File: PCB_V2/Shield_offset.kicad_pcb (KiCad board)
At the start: 4 copper layers, 83.2 x 79.4 mm, 120 parts, among them J1 ADC, J10 I2C, J11 SERVO3, J12 SERVO4, J13 Power OUT, J2 BATT, J3 PWR SW, J4 Screw_Terminal_01x04, J5 SERVO1, J6 ULTRA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

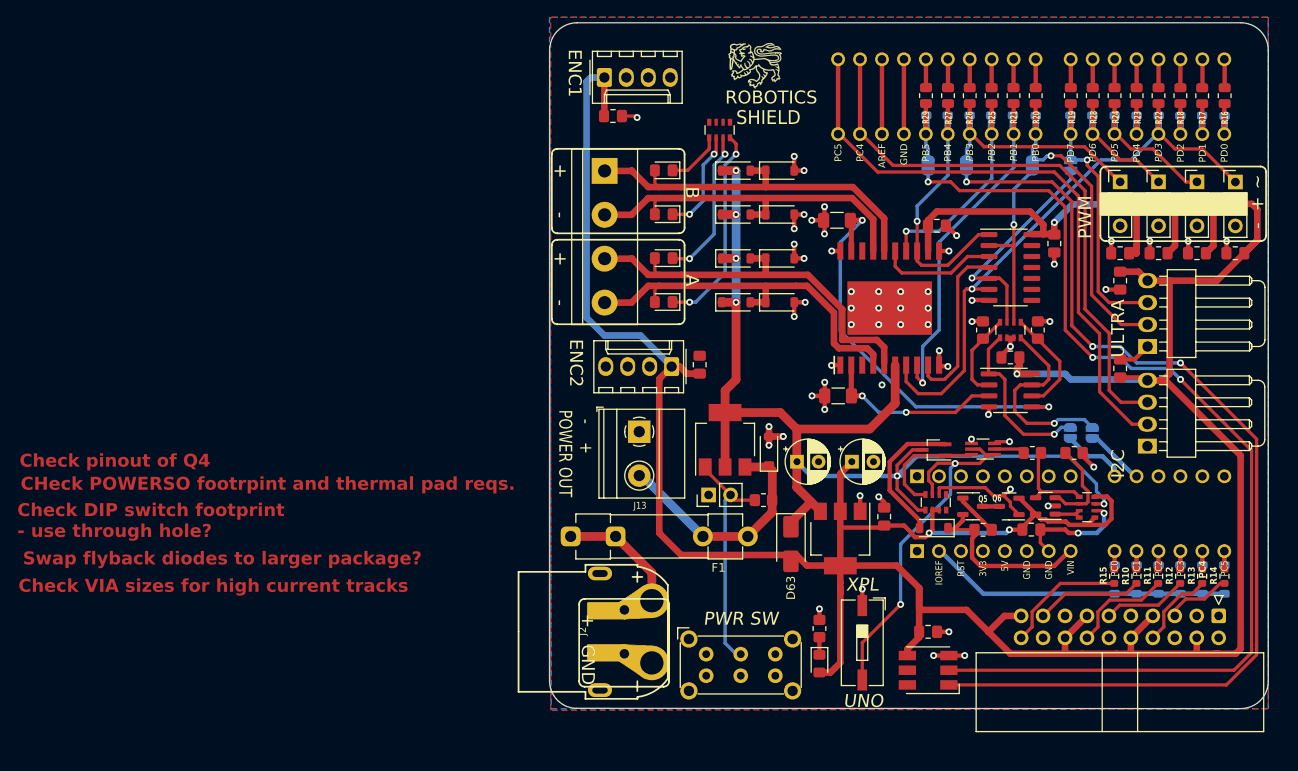
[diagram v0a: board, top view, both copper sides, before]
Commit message: Minor changes to layout
fixed overlapping silk and courtyards
tweaked track layouts to clear disconencted edges and imporve some clearances
fixed board outline
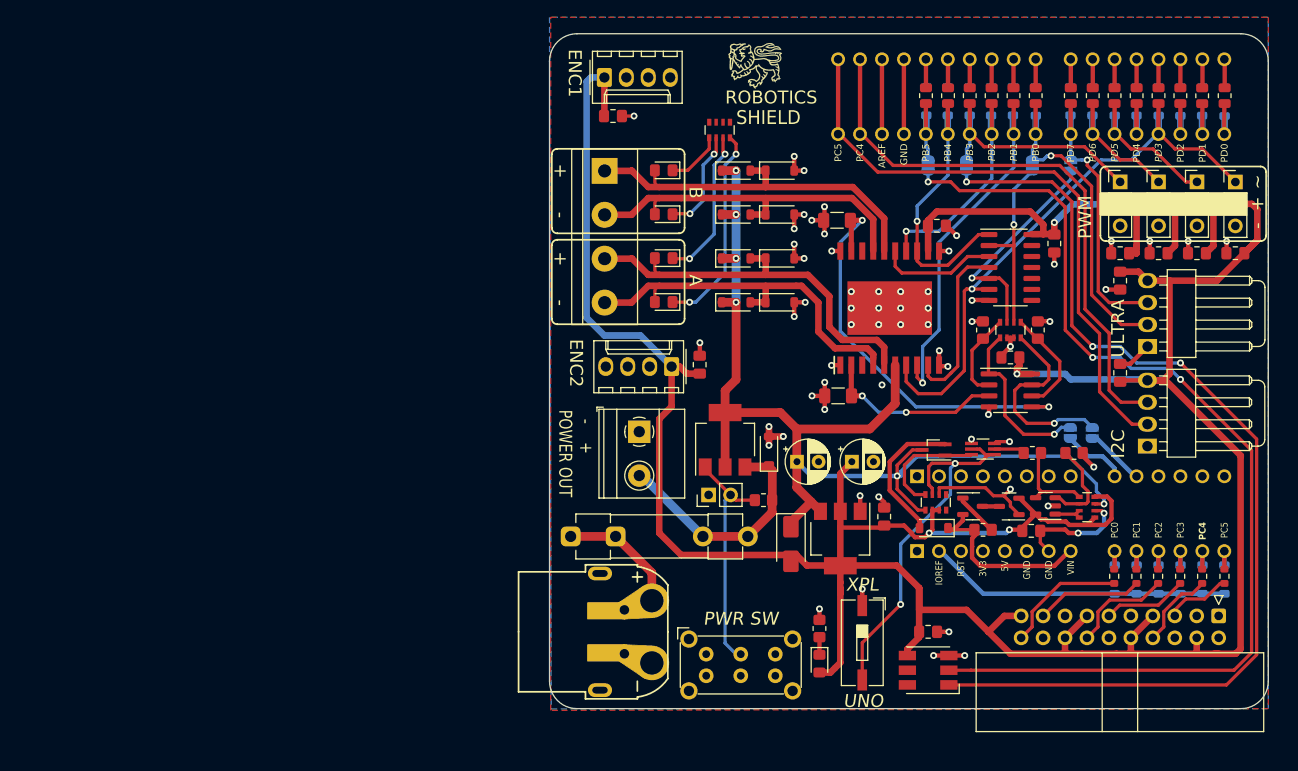
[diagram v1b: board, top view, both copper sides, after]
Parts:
- moved C12 0.51 mm to (158.8, 61.5)
- moved C6 0.15 mm to (148.5, 79.8)
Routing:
- net GND: track 107.7 -> 109.5 mm, vias 60 -> 61
- net /AIN5: track 10.2 -> 11.8 mm
- net /AIN3: track 10.4 -> 12.0 mm
- net /AIN2: track 10.4 -> 12.0 mm
- net /AIN0: track 18.1 -> 19.7 mm
- net /AIN1: track 17.4 -> 19.0 mm
- net /AIN4: track 10.8 -> 12.0 mm
- net /ENC2B: track 87.8 -> 88.9 mm
- net Net-(J3-Pin_2): track 27.7 -> 26.8 mm
- net +5V: track 408.0 -> 407.3 mm
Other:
- board size 83.2 x 79.4 mm -> 83.2 x 78.1 mm
- board text removed: "CHeck POWERSO footrpint and thermal pad reqs."
- board text removed: "Check DIP switch footprint - use through hole?"
- board text removed: "Check VIA sizes for high current tracks"
- board text removed: "Check pinout of Q4"
- board text removed: "Swap flyback diodes to larger package?"

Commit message: Update
Added gnd via's, and caps for LP filter on analog in's
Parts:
- added C17: NL, Capacitor_SMD:C_0805_2012Metric_Pad1.18x1.45mm_HandSolder, B.Cu at (158.8, 78.7)
- added C18: NL, Capacitor_SMD:C_0805_2012Metric_Pad1.18x1.45mm_HandSolder, B.Cu at (161.3, 78.7)
- added C19: NL, Capacitor_SMD:C_0805_2012Metric_Pad1.18x1.45mm_HandSolder, B.Cu at (163.8, 78.7)
- added C20: NL, Capacitor_SMD:C_0805_2012Metric_Pad1.18x1.45mm_HandSolder, B.Cu at (166.4, 78.7)
- added C21: NL, Capacitor_SMD:C_0805_2012Metric_Pad1.18x1.45mm_HandSolder, B.Cu at (168.9, 78.7)
- added C22: NL, Capacitor_SMD:C_0805_2012Metric_Pad1.18x1.45mm_HandSolder, B.Cu at (171.4, 78.7)
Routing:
- net /AIN3: track 12.0 -> 14.6 mm
- net /AIN2: track 12.0 -> 14.6 mm
- net /AIN4: track 12.0 -> 14.6 mm
- net /AIN0: track 19.7 -> 22.3 mm
- net /AIN5: track 11.8 -> 14.4 mm
- net /AIN1: track 19.0 -> 21.6 mm
- net GND: vias 61 -> 117

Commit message: updates
Bug fixes
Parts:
- removed J3: PWR SW, Connector_PinHeader_2.54mm:PinHeader_1x02_P2.54mm_Vertical
- C4: value C -> 100n
- D1, D11, D12, D13, D14, D15, D16, D2, D3, D5, D6, D7, D8, D9: value D -> SS14
- D21, D4: value D -> US1G
- J4: footprint TerminalBlock:TerminalBlock_bornier-4_P5.08mm -> TerminalBlock_Phoenix:TerminalBlock_Phoenix_MKDS-1,5-4-5.08_1x04_P5.08mm_Horizontal
- Q3: value Q_PMOS_GDS -> SSM3J356R; footprint Package_TO_SOT_SMD:SOT-323_SC-70_Handsoldering -> Package_TO_SOT_SMD:SOT-23-3
- moved J1 2.45 mm to (170.1, 92.0)
- moved C10 2.32 mm to (110.1, 58.2)
- moved J9 2.32 mm to (106.8, 58.4)
- moved J13 2.24 mm to (103.1, 66.0)
- moved D11 1.87 mm to (114.3, 46.4)
- moved D12 1.87 mm to (119.4, 46.4)
- moved D13 1.87 mm to (114.3, 41.3)
- moved D14 1.87 mm to (119.4, 41.3)
- moved D15 1.87 mm to (114.3, 36.2)
- moved D16 1.87 mm to (119.4, 36.2)
- moved D19 1.87 mm to (105.9, 41.2)
- moved D20 1.87 mm to (105.9, 36.2)
- moved J4 1.87 mm to (99.1, 36.2)
- moved RN3 1.87 mm to (112.4, 31.5)
- moved D17 1.87 mm to (105.9, 51.4)
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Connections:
- D21 pad 2: Net-(D21-A) -> unconnected-(D21-A-Pad2)
- J13 pad 2: Net-(D4-K) -> +BATT
- Q3 pad 2: Net-(D21-A) -> +BATT
- Q3 pad 3: +BATT -> Net-(D21-A)
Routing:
- net +BATT: track 134.4 -> 151.6 mm
- net +5V: track 407.6 -> 419.4 mm
- net Net-(D4-K): track 26.9 -> 16.6 mm
- net /ENC2A: track 90.3 -> 81.3 mm
- net Net-(J2-Pin_2): track 14.4 -> 17.7 mm
- net /AIN5: track 14.4 -> 17.5 mm
- net /AIN1: track 21.6 -> 24.7 mm
- net /AIN3: track 14.6 -> 17.7 mm
- net /AIN2: track 14.6 -> 17.7 mm
- net /AIN4: track 14.6 -> 17.7 mm
- net /AIN0: track 22.3 -> 25.2 mm
- net Net-(D22-CI): track 119.2 -> 122.0 mm
- net Net-(D21-A): track 16.4 -> 13.8 mm
- net Net-(D22-DI): track 117.6 -> 120.1 mm
- net /ENC2B: track 88.9 -> 86.6 mm
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
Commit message: V2 update
Foot prints, component selection, etc.
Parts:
- C2: footprint Capacitor_THT:CP_Radial_D5.0mm_P2.50mm -> Capacitor_SMD:CP_Elec_6.3x7.7
- C5: footprint Capacitor_THT:CP_Radial_D5.0mm_P2.50mm -> Capacitor_SMD:CP_Elec_6.3x5.7
- D1, D2, D3, D5, D6, D7: value SS14 -> CDBW140-G
- D11, D12, D13, D14, D15, D16, D21, D4, D8, D9: footprint Diode_SMD:D_SOD-123 -> Diode_SMD:D_SMA
- U2: value NCP1117-5.0_SOT223 -> MCT1117C-5.0-TP
- U4: footprint Package_TO_SOT_SMD:SOT-23-5 -> Package_TO_SOT_SMD:SOT-353_SC-70-5
- moved D4 10.7 mm to (115.7, 60.1)
- moved R1 2.91 mm to (114.6, 74.9)
- moved C5 1.89 mm to (128.6, 70.1), turned to 90 degrees
- moved D11 1.81 mm to (112.5, 46.4)
- moved D13 1.81 mm to (112.5, 41.3)
- moved D15 1.81 mm to (112.5, 36.2)
- moved D8 1.81 mm to (112.5, 51.4)
- moved C2 1.63 mm to (121.4, 70.1), turned to -90 degrees
- moved D12 0.54 mm to (119.9, 46.4)
- moved D14 0.54 mm to (119.9, 41.3)
- moved D16 0.54 mm to (119.9, 36.2)
- moved D9 0.54 mm to (119.9, 51.4)
- moved RN4 0.38 mm to (137.4, 76.1)
- moved Q3 0.13 mm to (137.0, 69.8)
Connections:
- D21 pad 2: unconnected-(D21-A-Pad2) -> Net-(D21-A)
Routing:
- net Net-(D4-K): track 16.6 -> 27.4 mm, vias 0 -> 4
- net Net-(D17-A): track 58.4 -> 47.8 mm
- net +5V: track 419.4 -> 425.2 mm, vias 4 -> 5
- net +BATT: track 151.6 -> 147.4 mm, vias 6 -> 8
- net Net-(Q1-G): track 26.7 -> 23.3 mm
- net Net-(D11-A): track 48.2 -> 50.2 mm
- net GND: track 109.5 -> 111.3 mm, vias 114 -> 135
- net Net-(D18-K): track 17.8 -> 19.5 mm
- net Net-(D15-A): track 45.0 -> 46.7 mm
- net Net-(D13-A): track 43.3 -> 44.9 mm
- net Net-(D17-K): track 23.9 -> 25.3 mm
- net /ENC2A: track 81.3 -> 82.4 mm
- net Net-(D19-K): track 12.0 -> 13.1 mm
- net Net-(Q2B-D): track 20.5 -> 21.3 mm

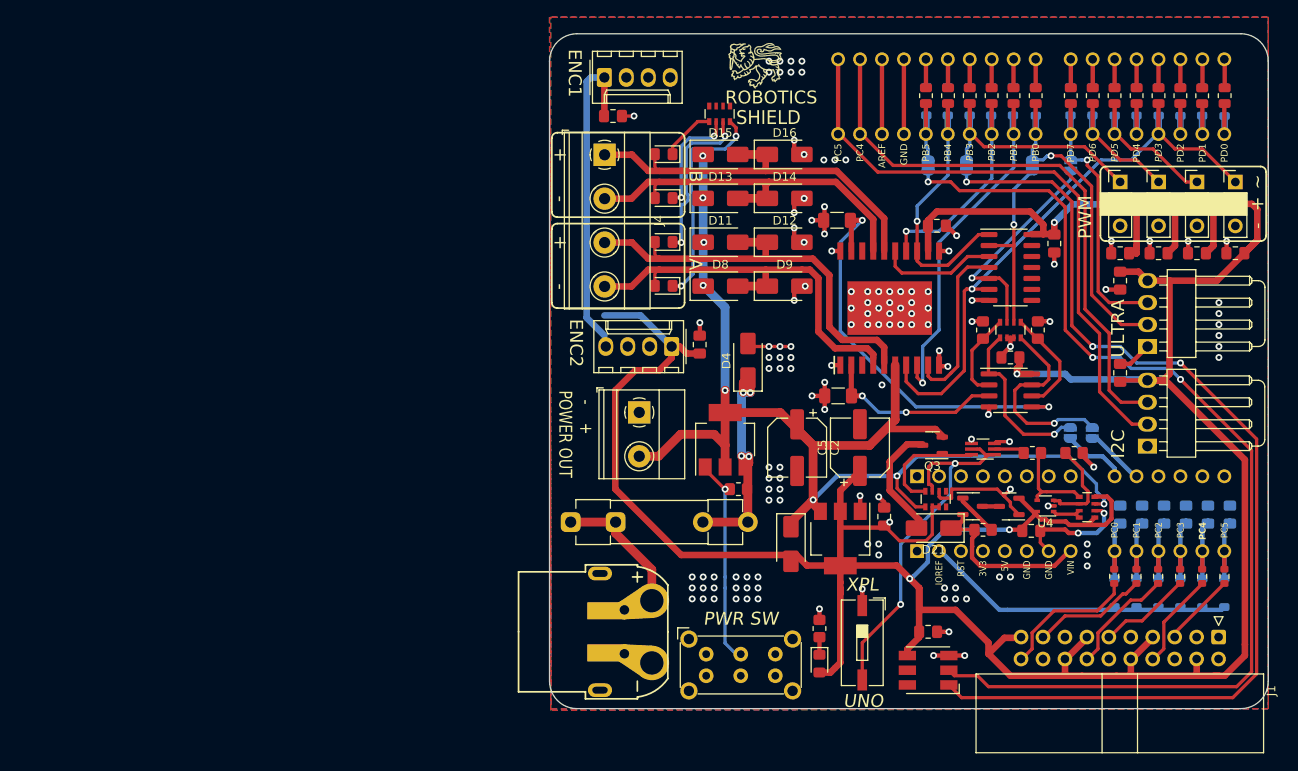
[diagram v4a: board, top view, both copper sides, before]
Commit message: Minor changes to layout
Made placement of connectors more consistent.
Relocated SMT electrolytic caps to allow more space
Made IN1 layer 5V
Tidied routing of motor driver outputs and swapped to using pours. Moved vias out from under components.
Adjusted power supply component placement to allow more space and smaller loop areas.
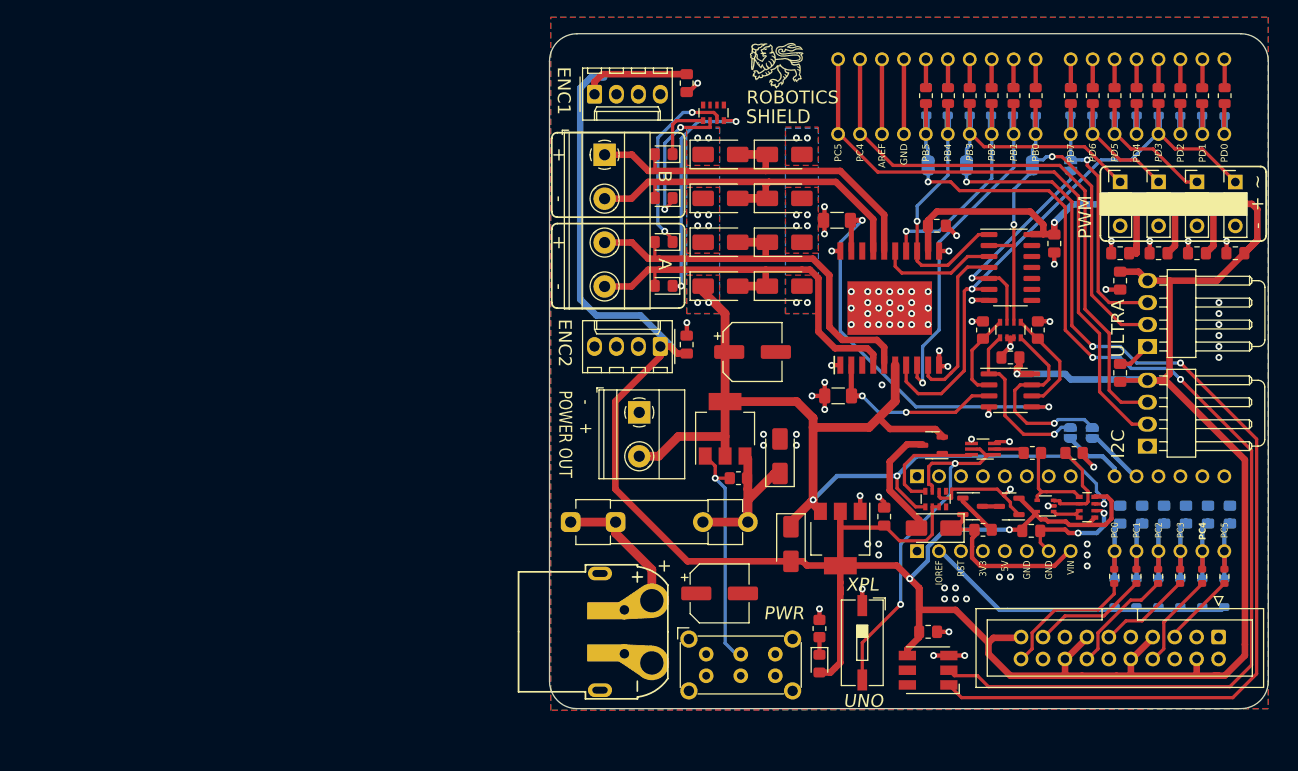
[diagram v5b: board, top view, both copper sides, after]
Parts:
- J1: footprint Connector_IDC:IDC-Header_2x10_P2.54mm_Horizontal -> Connector_IDC:IDC-Header_2x10_P2.54mm_Vertical
- moved C5 23.4 mm to (112.4, 87.0), turned to 0 degrees
- moved C2 12.2 mm to (116.2, 59.1), turned to 0 degrees
- moved D4 11.6 mm to (119.4, 71.1)
- moved C8 9.34 mm to (108.6, 27.9), turned to -90 degrees
- moved J7 2.26 mm to (97.9, 29.2)
- moved C10 1.50 mm to (108.6, 58.2)
- moved J9 1.31 mm to (105.5, 58.4)
- moved Q1 1.27 mm to (113.0, 67.9)
- moved R1 1.27 mm to (114.6, 73.7)
- moved RN3 0.71 mm to (111.7, 31.4)
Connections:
- net ~Reset renamed ~{RESET}
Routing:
- net +BATT: track 147.4 -> 126.7 mm, vias 8 -> 11
- net GND: track 111.3 -> 97.6 mm, vias 135 -> 92
- net Net-(D4-K): track 27.4 -> 20.5 mm, vias 4 -> 0
- net /ENC2A: track 82.4 -> 87.6 mm
- net Net-(D19-K): track 13.1 -> 16.2 mm
- net Net-(Q1-G): track 23.3 -> 26.1 mm
- net /ENC1A: track 76.1 -> 78.6 mm
- net /ENC1B: track 76.1 -> 78.2 mm
- net Net-(D18-K): track 19.5 -> 21.5 mm
- net +5V: track 425.2 -> 423.6 mm, vias 5 -> 4
- net Net-(D17-K): track 25.3 -> 26.7 mm
- net Net-(D20-K): track 6.32 -> 7.15 mm
- added copper zone on In1.Cu, net +5V
- added copper zone on B.Cu, net +BATT
- added copper zone on F.Cu, net +BATT
- removed copper zone on In1.Cu, net GND
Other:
- board text added: "PWR"
